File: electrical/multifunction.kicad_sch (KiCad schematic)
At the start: 30 parts

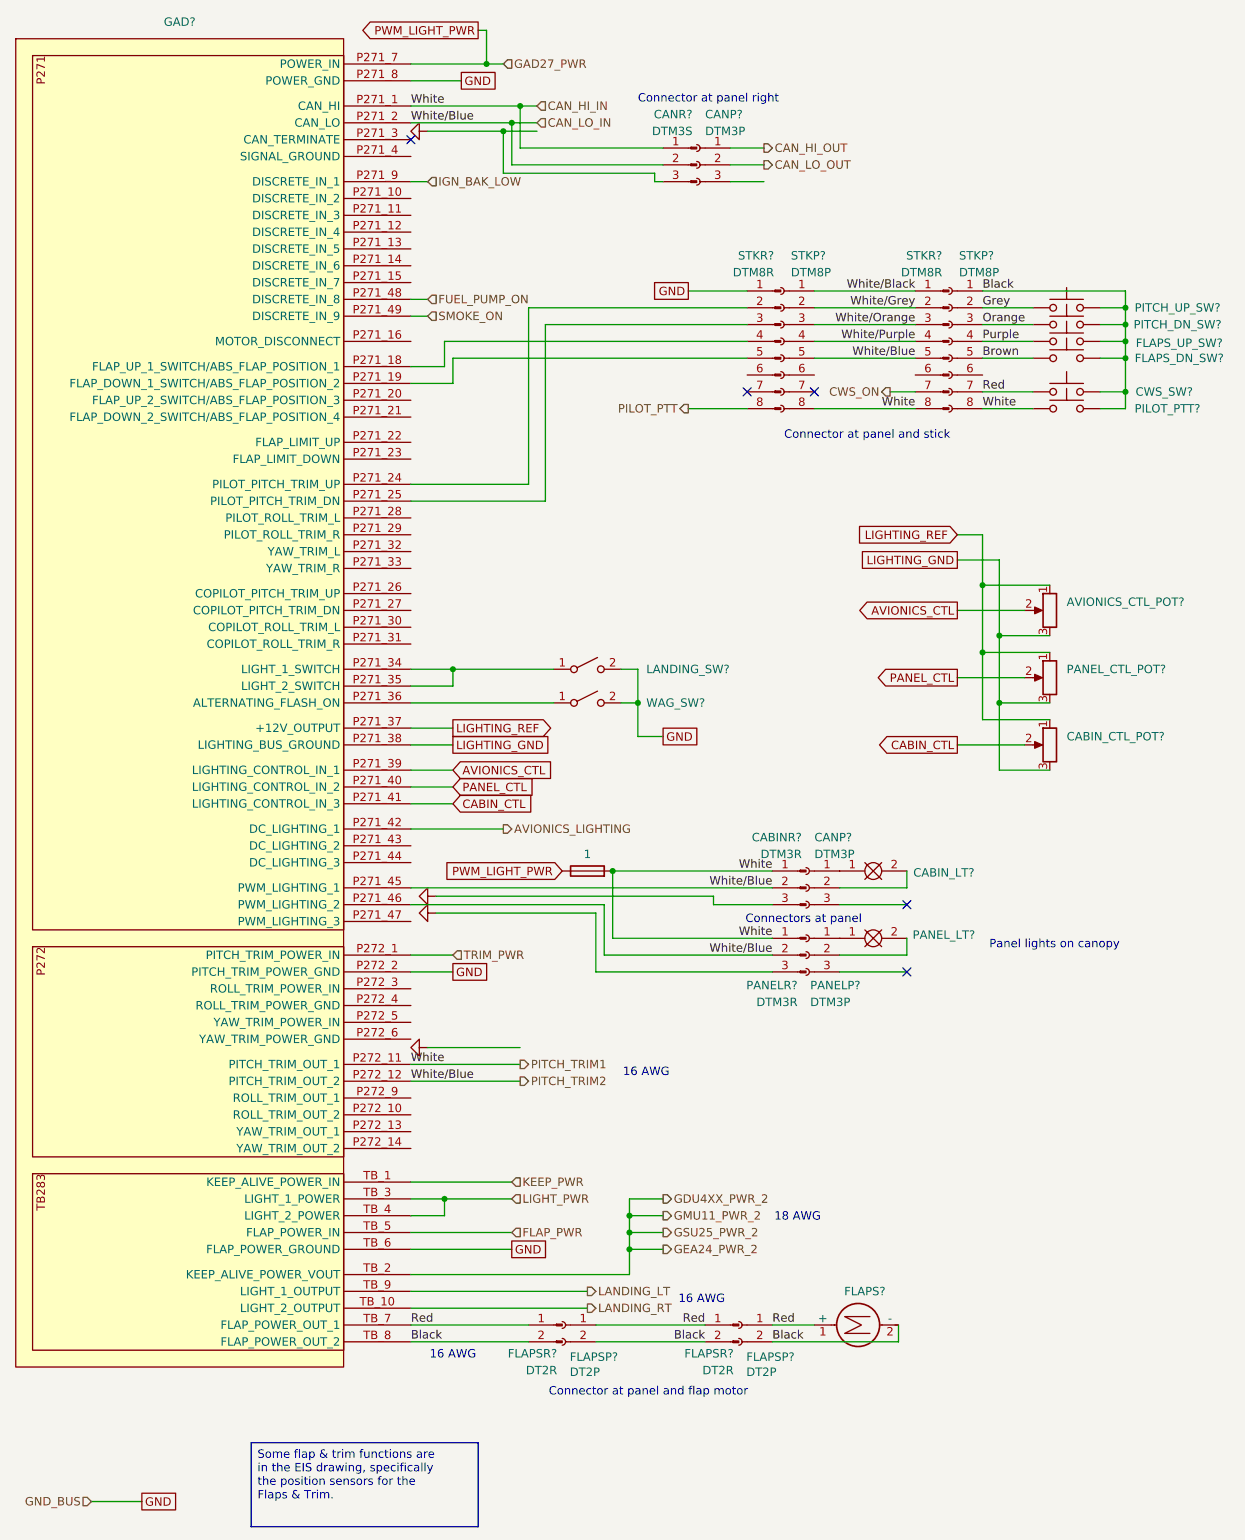
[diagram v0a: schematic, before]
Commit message: Upgraded G3X Touch to Axis
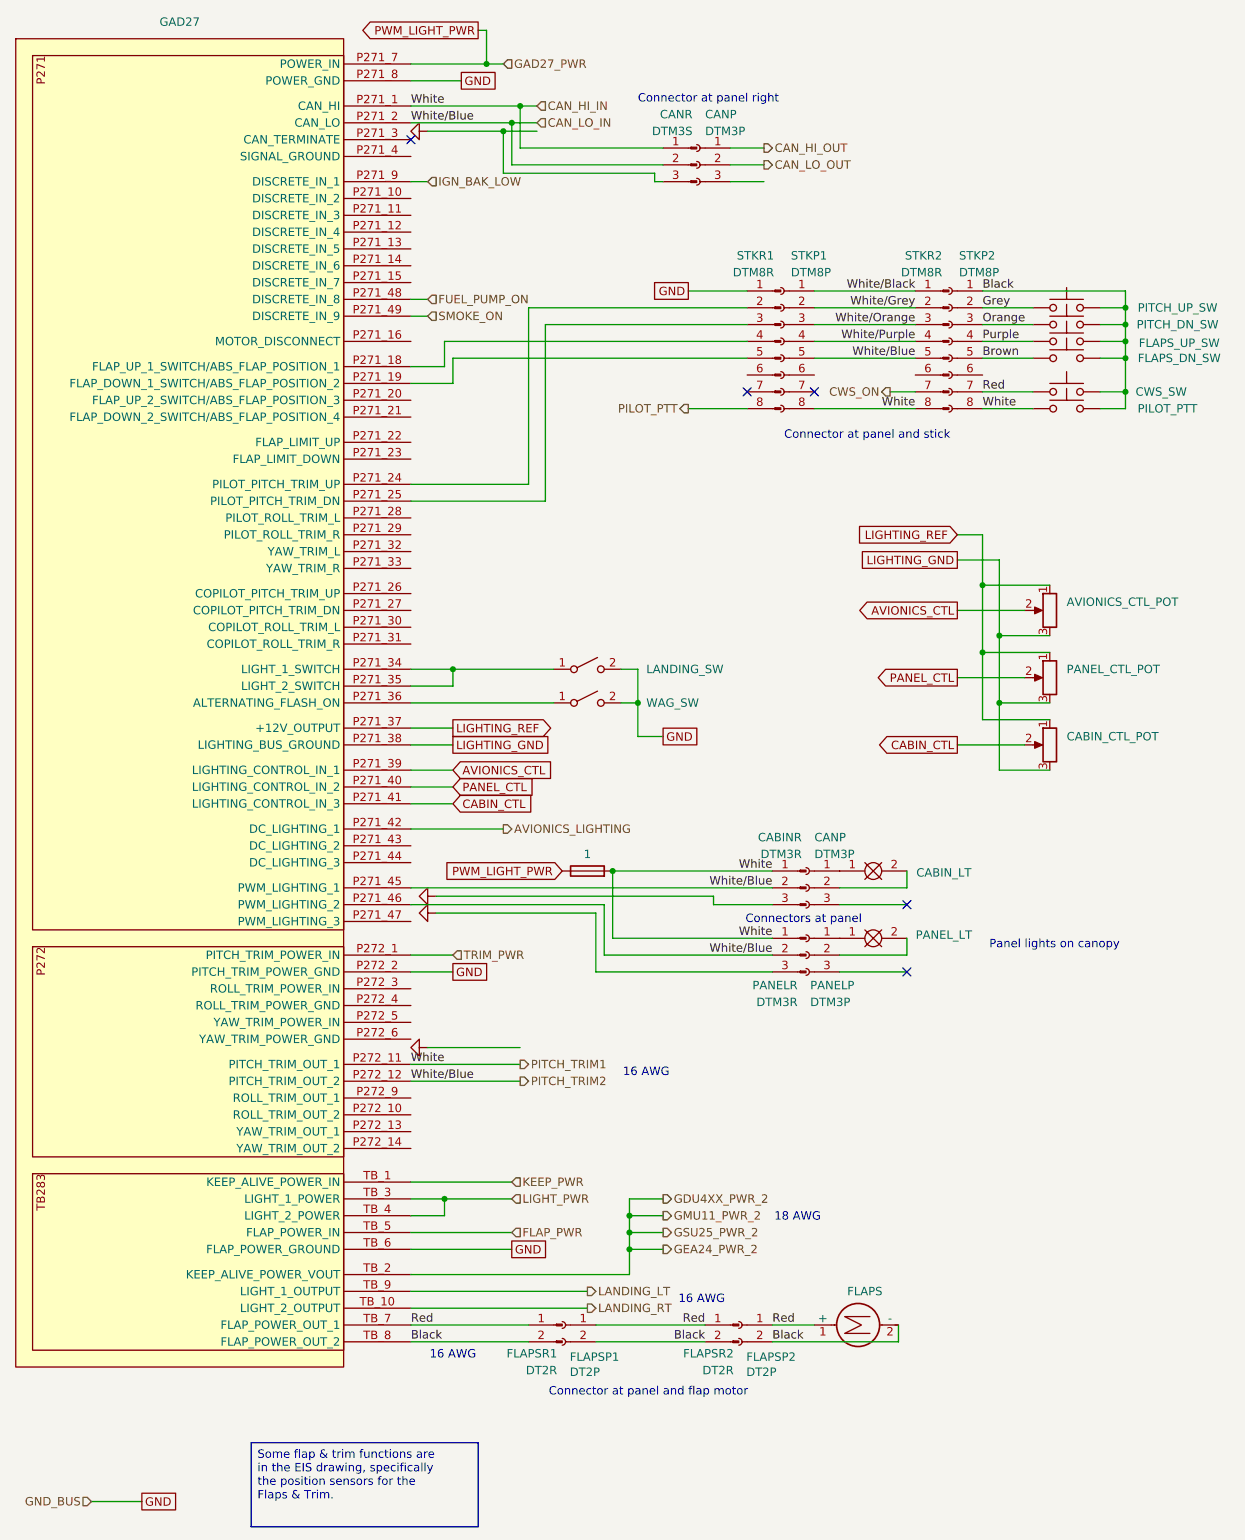
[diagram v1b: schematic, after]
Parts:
- CABIN_LT: renamed from CABIN_LT?; value ~ -> (none)
- GAD27: renamed from GAD?; value ~ -> (none)
- LANDING_SW: renamed from LANDING_SW?; value ~ -> (none)
- PANEL_LT: renamed from PANEL_LT?; value ~ -> (none)
- WAG_SW: renamed from WAG_SW?; value ~ -> (none)
- gave numbers to parts that had none: 24
